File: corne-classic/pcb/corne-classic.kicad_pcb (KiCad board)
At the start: 2 copper layers, 133.8 x 92.2 mm, 98 parts, among them J1 MJ-4PP-9, J2 OLED, J3 LED, P1 i2c-pin, P2 i2c-pin, SW1 SW_PUSH, SW10 SW_PUSH, SW11 SW_PUSH, SW12 SW_PUSH, SW13 SW_PUSH, SW14 SW_PUSH, SW15 SW_PUSH, SW16 SW_PUSH, SW17 SW_PUSH, SW18 SW_PUSH, SW19 SW_PUSH, SW2 SW_PUSH, SW20 SW_PUSH, SW21 SW_PUSH, SW3 SW_PUSH, SW4 SW_PUSH, SW5 SW_PUSH, SW6 SW_PUSH, SW7 SW_PUSH, SW8 SW_PUSH, SW9 SW_PUSH, U1 ProMicro

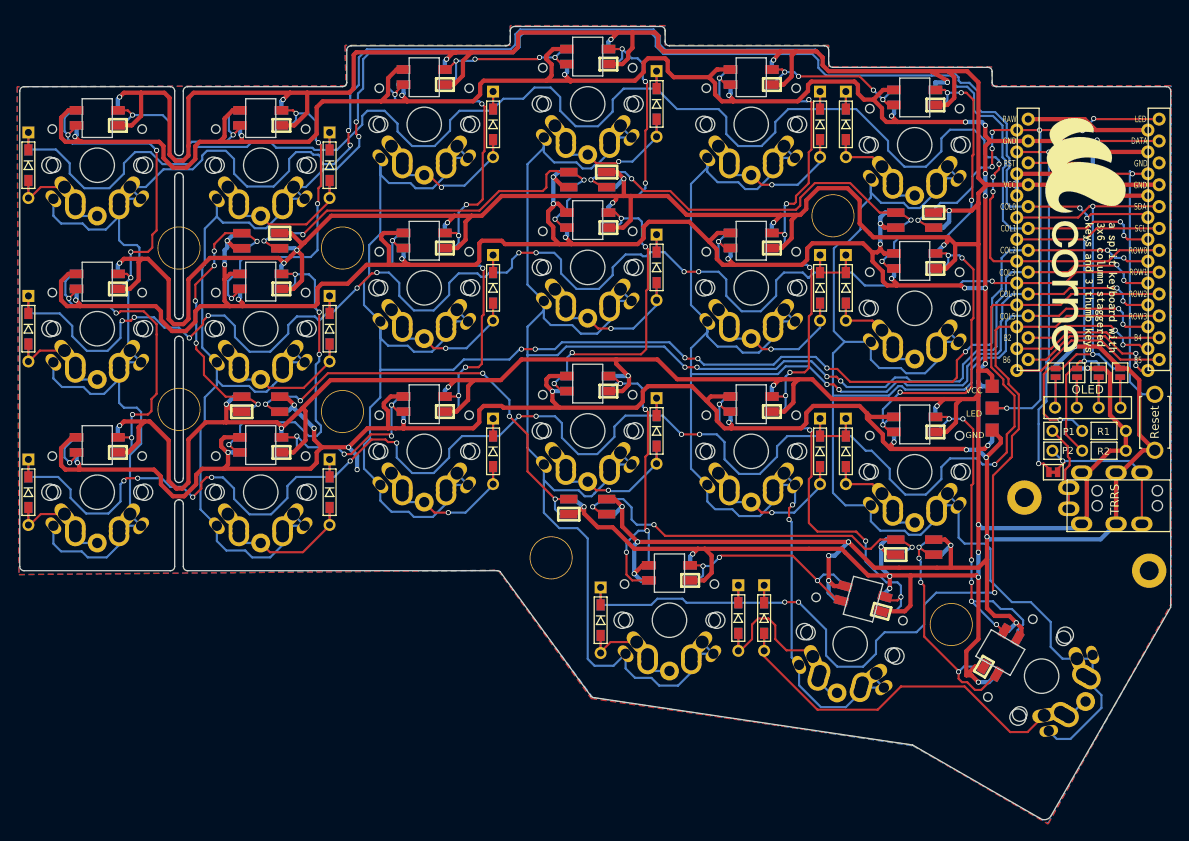
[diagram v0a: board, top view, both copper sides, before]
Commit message: remove snap off area
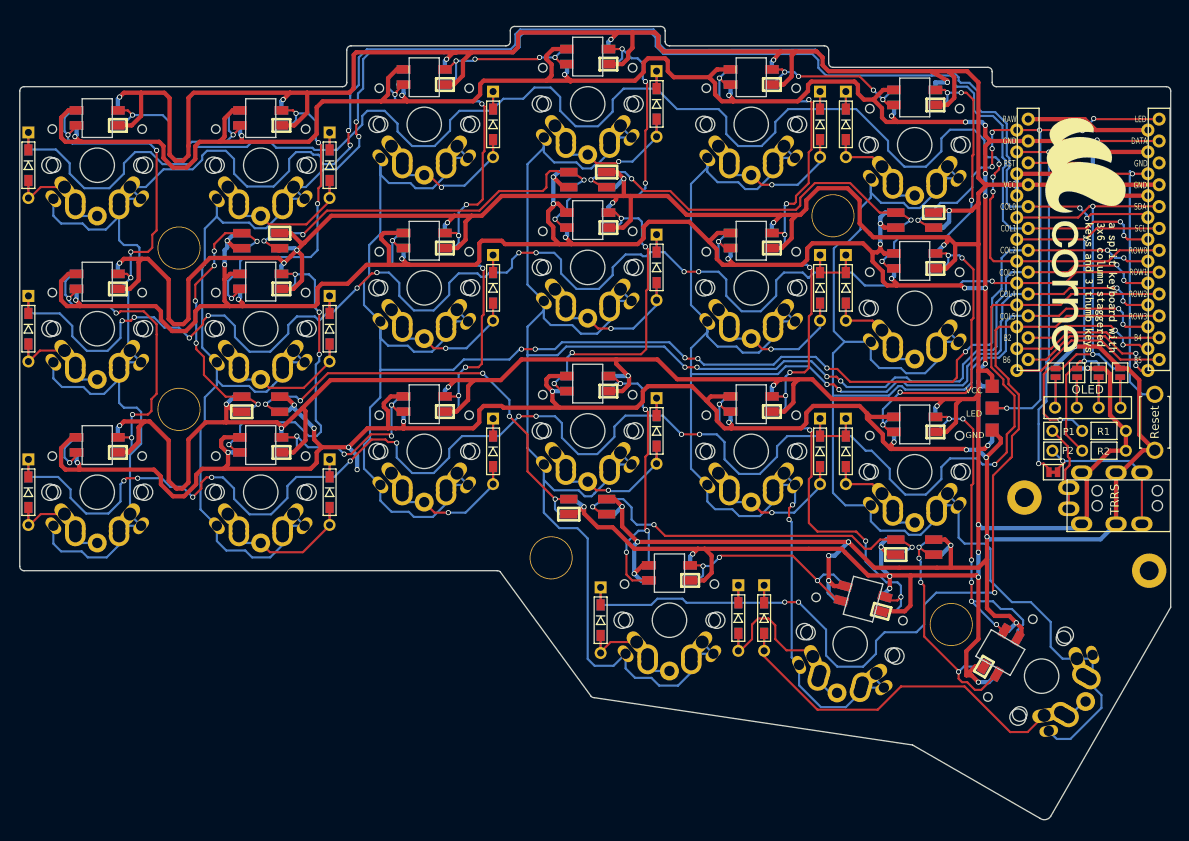
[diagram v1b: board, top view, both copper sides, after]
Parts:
- removed the ? at (98.5, 86.8)
- removed the ? at (98.5, 105.8)
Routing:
- removed copper zone on B.Cu, net GND
- removed copper zone on F.Cu, net GND
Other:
- outline, holes or cut-outs redrawn

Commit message: removed OLED and LEDs
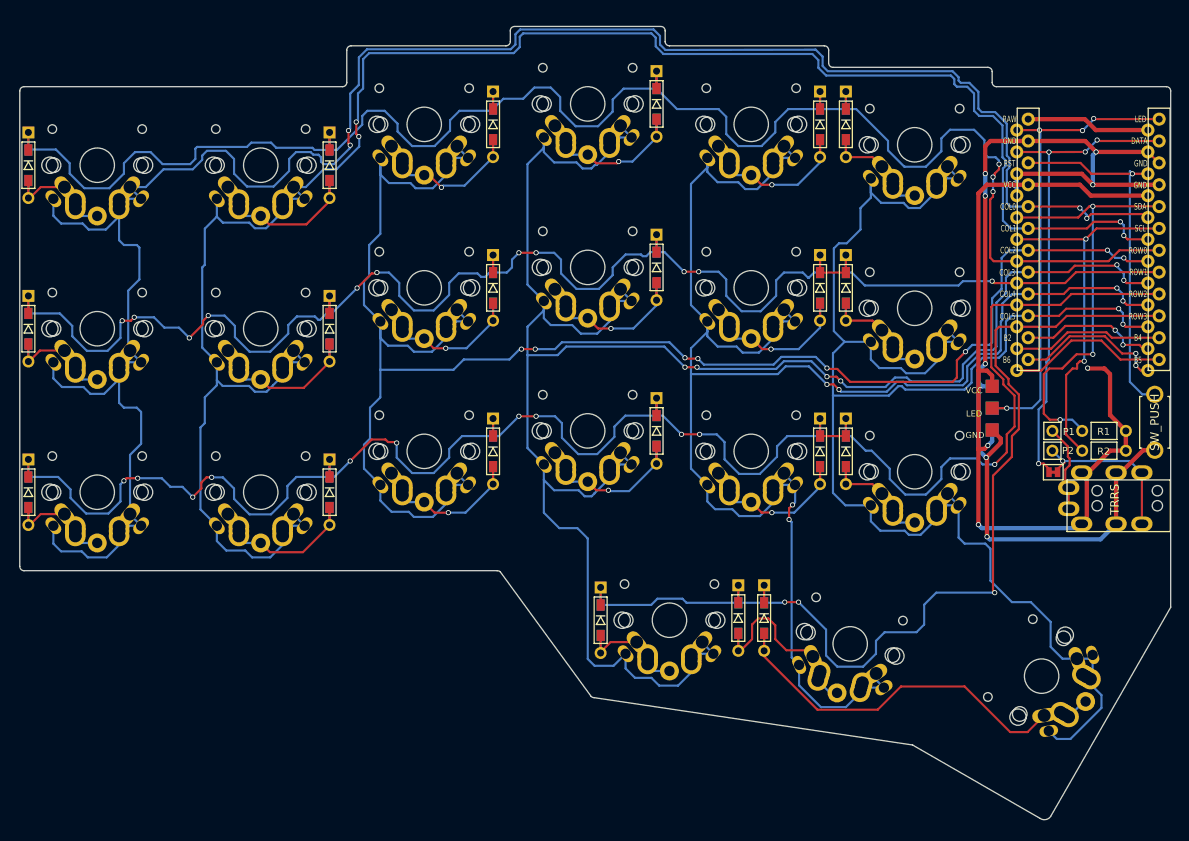
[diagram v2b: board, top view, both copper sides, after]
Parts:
- removed ? (x7): , kbd:LEGO_HOLE
- removed G*** (x2): LOGO, kbd:corne
- removed J2: OLED, kbd:OLED
- removed JP2, JP3, JP4, JP5, JP6, JP7, JP8, JP9: , kbd:Jumper
- removed L1, L2, L3, L4, L5, L6: SK6812MINI, kbd:SK6812MINI_underglow_rev
- removed L10, L11, L12, L13, L14, L15, L16, L17, L18, L19, L20, L21, L22, L23, L24, L25, L26, L27, L7, L8, L9: SK6812MINI, kbd:SK6812MINI_rev
- RSW1: value Reset -> SW_PUSH
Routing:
- net GND: track 797.7 -> 124.8 mm, vias 49 -> 7
- net VCC: track 758.8 -> 103.1 mm, vias 33 -> 3
- net Net-(L25-Pad1): track 52.1 -> 0.00 mm, vias 5 -> 0
- net Net-(L17-Pad1): track 49.6 -> 0.00 mm, vias 4 -> 0
- net Net-(L23-Pad3): track 48.0 -> 0.00 mm, vias 3 -> 0
- net Net-(L22-Pad3): track 46.7 -> 0.00 mm, vias 3 -> 0
- net Net-(L26-Pad1): track 45.8 -> 0.00 mm, vias 3 -> 0
- net Net-(L18-Pad3): track 41.9 -> 0.00 mm, vias 6 -> 0
- net Net-(L14-Pad1): track 40.5 -> 0.00 mm, vias 4 -> 0
- net Net-(L2-Pad3): track 39.4 -> 0.00 mm, vias 4 -> 0
- net Net-(L3-Pad1): track 38.7 -> 0.00 mm, vias 4 -> 0
- net Net-(L11-Pad1): track 38.7 -> 0.00 mm, vias 4 -> 0
- net Net-(L15-Pad3): track 38.5 -> 0.00 mm, vias 4 -> 0
- net Net-(L11-Pad3): track 38.2 -> 0.00 mm, vias 4 -> 0
- net Net-(L12-Pad3): track 38.2 -> 0.00 mm, vias 4 -> 0
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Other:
- outline, holes or cut-outs redrawn
- board text removed: "OLED"

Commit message: staggered pinky
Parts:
- moved D1 1.00 mm to (62.0, 78.1)
- moved D13 1.00 mm to (62.0, 116.1)
- moved D14 1.00 mm to (97.0, 116.1)
- moved D2 1.00 mm to (97.0, 78.1)
- moved D7 1.00 mm to (62.0, 97.1)
- moved D8 1.00 mm to (97.0, 97.1)
- moved SW1 1.00 mm to (70.0, 78.1)
- moved SW13 1.00 mm to (70.0, 116.1)
- moved SW14 1.00 mm to (89.0, 116.1)
- moved SW2 1.00 mm to (89.0, 78.1)
- moved SW7 1.00 mm to (70.0, 97.1)
- moved SW8 1.00 mm to (89.0, 97.1)
- moved SW11 0.88 mm to (146.0, 90.5)
- moved SW17 0.88 mm to (146.0, 109.5)
- moved SW5 0.88 mm to (146.0, 71.5)
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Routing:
- net col0: track 245.7 -> 249.3 mm
- net col1: track 221.3 -> 224.8 mm
- net col4: track 194.3 -> 195.7 mm
- net row2: track 215.8 -> 216.9 mm
- net row1: track 191.7 -> 192.7 mm
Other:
- board size 133.8 x 92.2 mm -> 133.8 x 93.2 mm

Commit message: added credits
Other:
- board text added: "Corne Classic v2.0 foostan ft. wy35"
- board text added: "Corne Classic v2.0 foostan ft. wy5"
- board text removed: "Corne Classic v2.0 PCB Designed by foostan"
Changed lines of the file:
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@@
     (34 B.Paste user hide)
     (35 F.Paste user hide)
-    (36 B.SilkS user hide)
-    (37 F.SilkS user hide)
-    (38 B.Mask user hide)
-    (39 F.Mask user hide)
+    (36 B.SilkS user)
+    (37 F.SilkS user)
+    (38 B.Mask user)
+    (39 F.Mask user)
     (40 Dwgs.User user hide)
     (41 Cmts.User user hide)
@@
   )
   (target plus (at 194.8 63.4) (size 5) (width 0.15) (layer Edge.Cuts))
-  (gr_text "Corne Classic v2.0\nPCB Designed by foostan" (at 119.4 121.5) (layer B.Mask)
+  (gr_text "Corne Classic v2.0\nfoostan ft. wy35\n" (at 119.4 121.5) (layer B.Mask)
     (effects (font (size 1 1) (thickness 0.125)) (justify left mirror))
   )
-  (gr_text "Corne Classic v2.0\nPCB Designed by foostan" (at 100.1 121.5) (layer F.Mask)
+  (gr_text "Corne Classic v2.0\nfoostan ft. wy5" (at 100.1 121.5) (layer F.Mask)
     (effects (font (size 1 1) (thickness 0.125)) (justify left))
   )

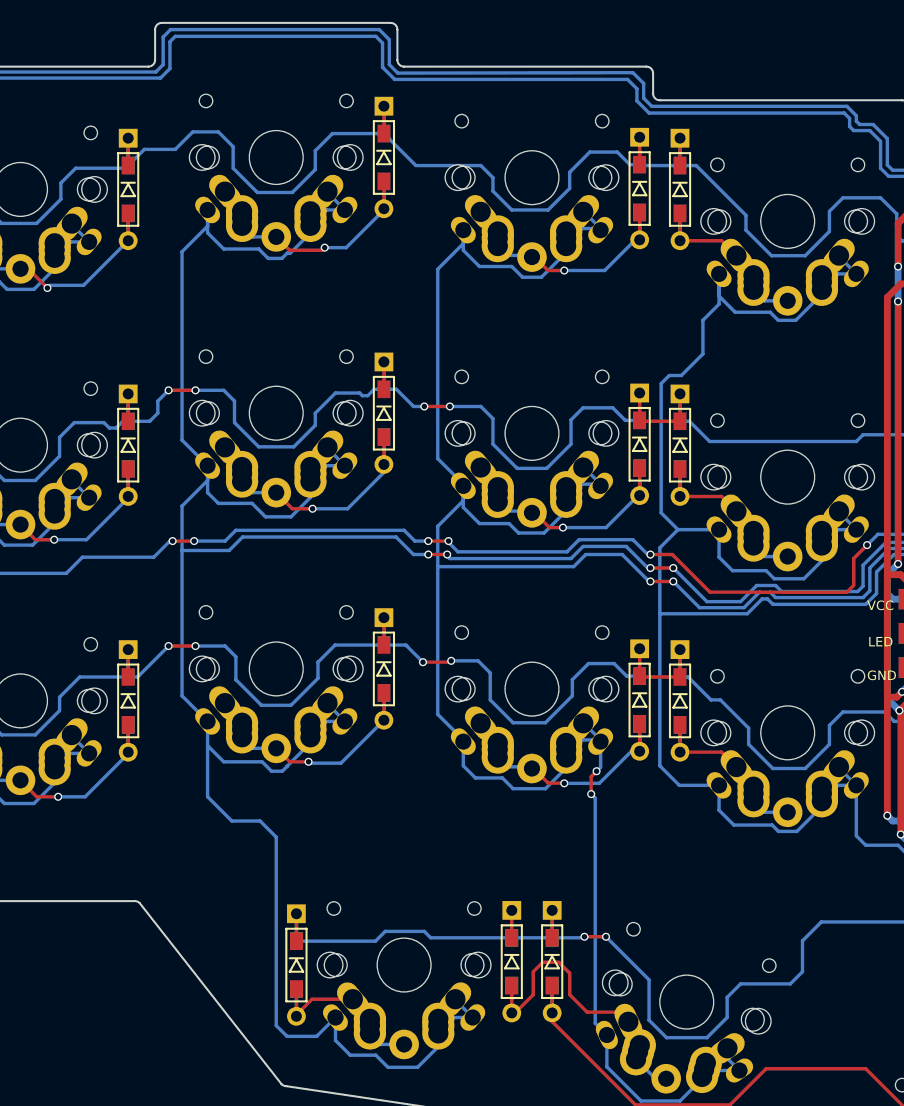
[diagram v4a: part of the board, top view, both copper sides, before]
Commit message: fixed columnar stagger
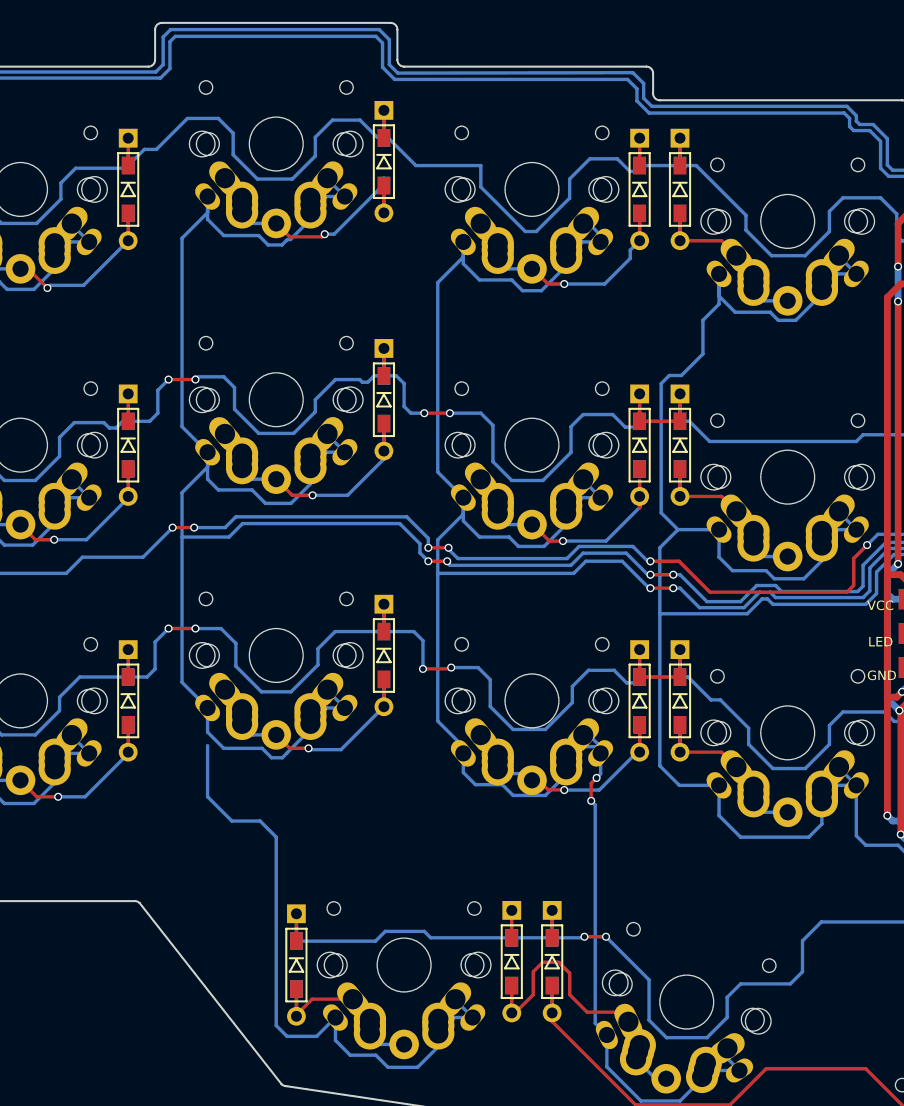
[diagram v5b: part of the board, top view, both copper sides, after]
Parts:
- moved D10 1.00 mm to (135.0, 88.0)
- moved D16 1.00 mm to (135.0, 107.0)
- moved SW10 1.00 mm to (127.0, 88.0)
- moved SW16 1.00 mm to (127.0, 107.0)
- moved SW4 1.00 mm to (127.0, 69.0)
- moved SW11 0.88 mm to (146.0, 91.4)
- moved SW17 0.88 mm to (146.0, 110.4)
- moved SW5 0.88 mm to (146.0, 72.4)
- moved D4 0.31 mm to (135.0, 70.3)
- moved D11 0.06 mm to (154.0, 91.4)
- moved D17 0.06 mm to (154.0, 110.4)
- moved D5 0.06 mm to (154.0, 72.4)
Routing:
- net row2: track 216.9 -> 220.6 mm
- net row1: track 192.7 -> 195.9 mm
- net row0: track 205.9 -> 208.5 mm
- net col5: track 187.0 -> 188.7 mm
- net col2: track 197.3 -> 198.5 mm
- net col4: track 195.7 -> 194.6 mm
- net col3: track 225.3 -> 226.1 mm
- net Net-(D5-Pad2): track 20.2 -> 20.8 mm

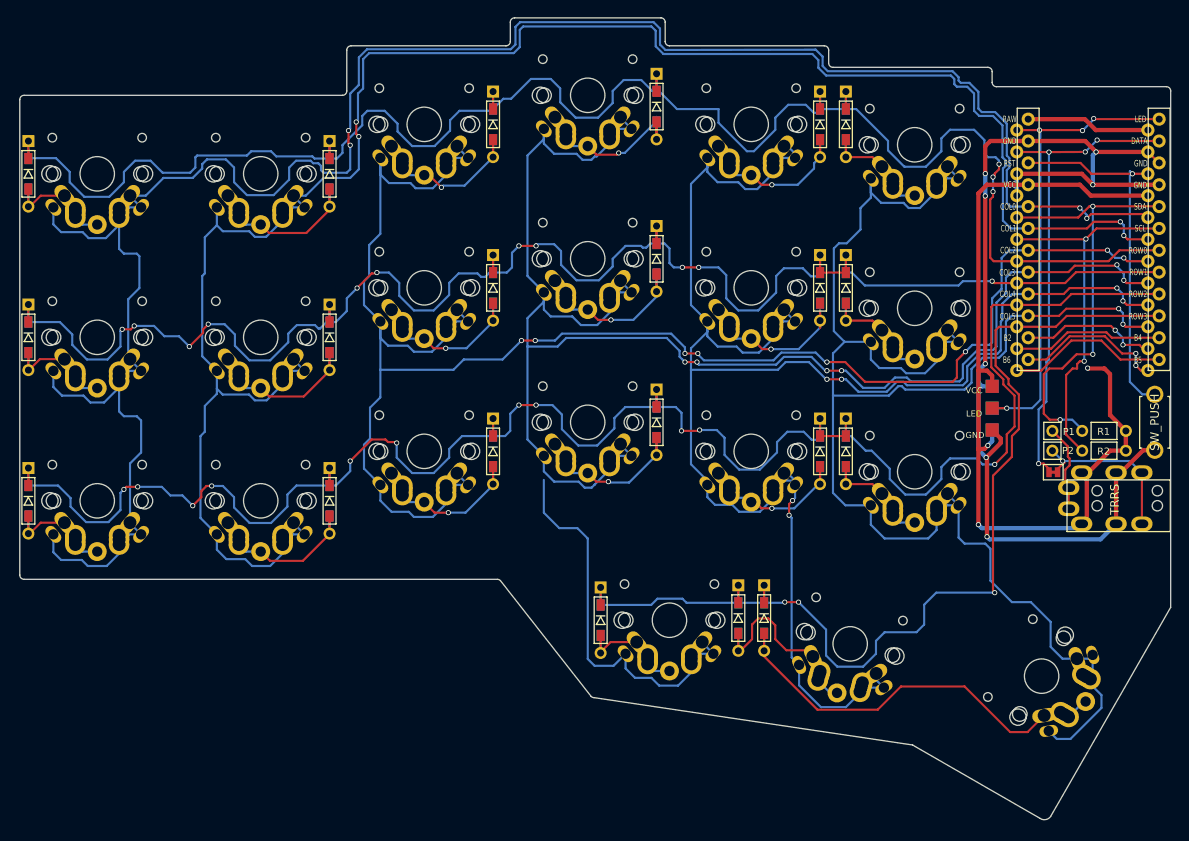
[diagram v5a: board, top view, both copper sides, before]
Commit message: moved pinkie 1 more row
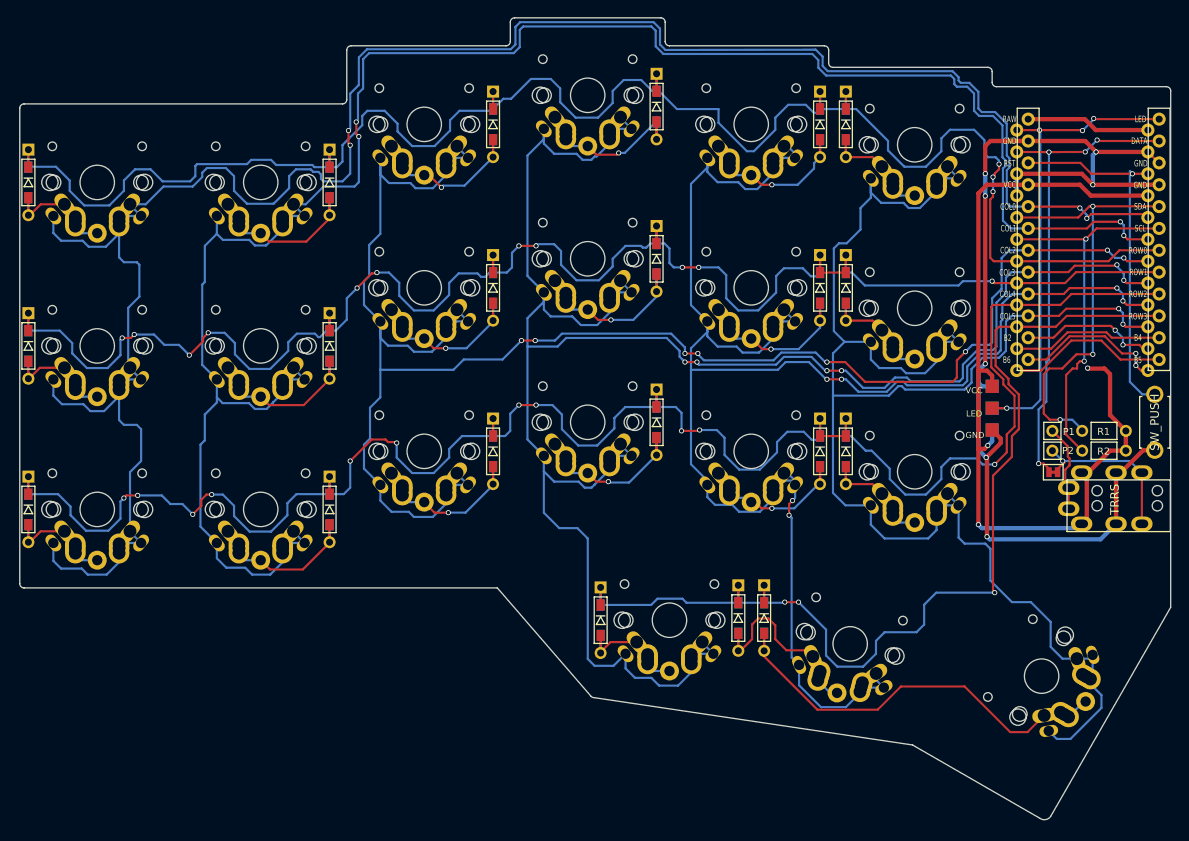
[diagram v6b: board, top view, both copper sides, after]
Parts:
- moved D1 1.00 mm to (62.0, 79.1)
- moved D13 1.00 mm to (62.0, 117.1)
- moved D14 1.00 mm to (97.0, 117.1)
- moved D2 1.00 mm to (97.0, 79.1)
- moved D7 1.00 mm to (62.0, 98.1)
- moved D8 1.00 mm to (97.0, 98.1)
- moved SW1 1.00 mm to (70.0, 79.1)
- moved SW13 1.00 mm to (70.0, 117.1)
- moved SW14 1.00 mm to (89.0, 117.1)
- moved SW2 1.00 mm to (89.0, 79.1)
- moved SW7 1.00 mm to (70.0, 98.1)
- moved SW8 1.00 mm to (89.0, 98.1)
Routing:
- net row2: track 220.6 -> 222.1 mm
- net col1: track 224.8 -> 226.1 mm
- net row1: track 195.9 -> 196.9 mm
- net row0: track 208.5 -> 209.5 mm
- net col3: track 226.1 -> 227.1 mm
- net col0: track 249.3 -> 250.0 mm
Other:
- outline, holes or cut-outs redrawn
